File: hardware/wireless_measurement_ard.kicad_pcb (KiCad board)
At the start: 4 copper layers, 30.3 x 17.8 mm, 25 parts, among them J1 Conn_01x08, SW1 SW_SPDT, U1 EFM8LB1, U2 JDY-08, U3 MCP16415, U4 MAX44284, U5 DRV5021

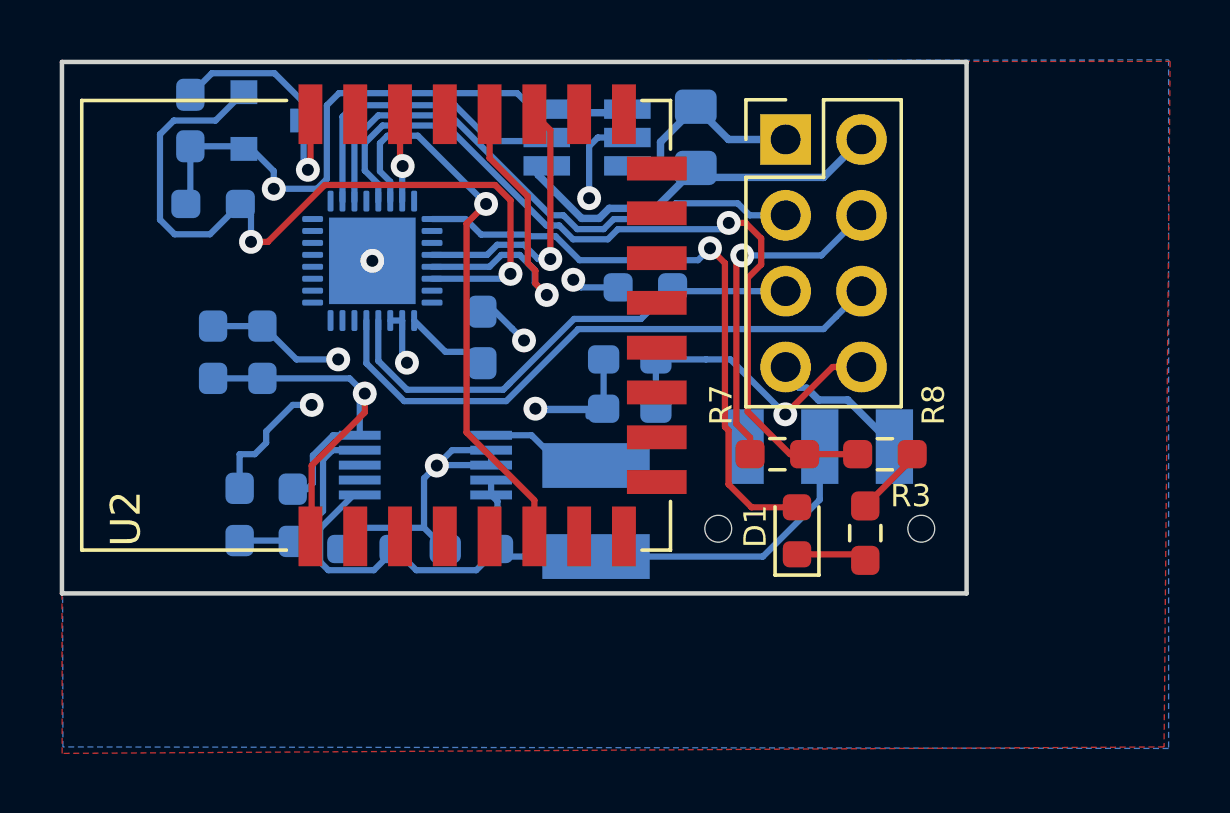
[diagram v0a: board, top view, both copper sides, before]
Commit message: Rerouting to remove components below antenna
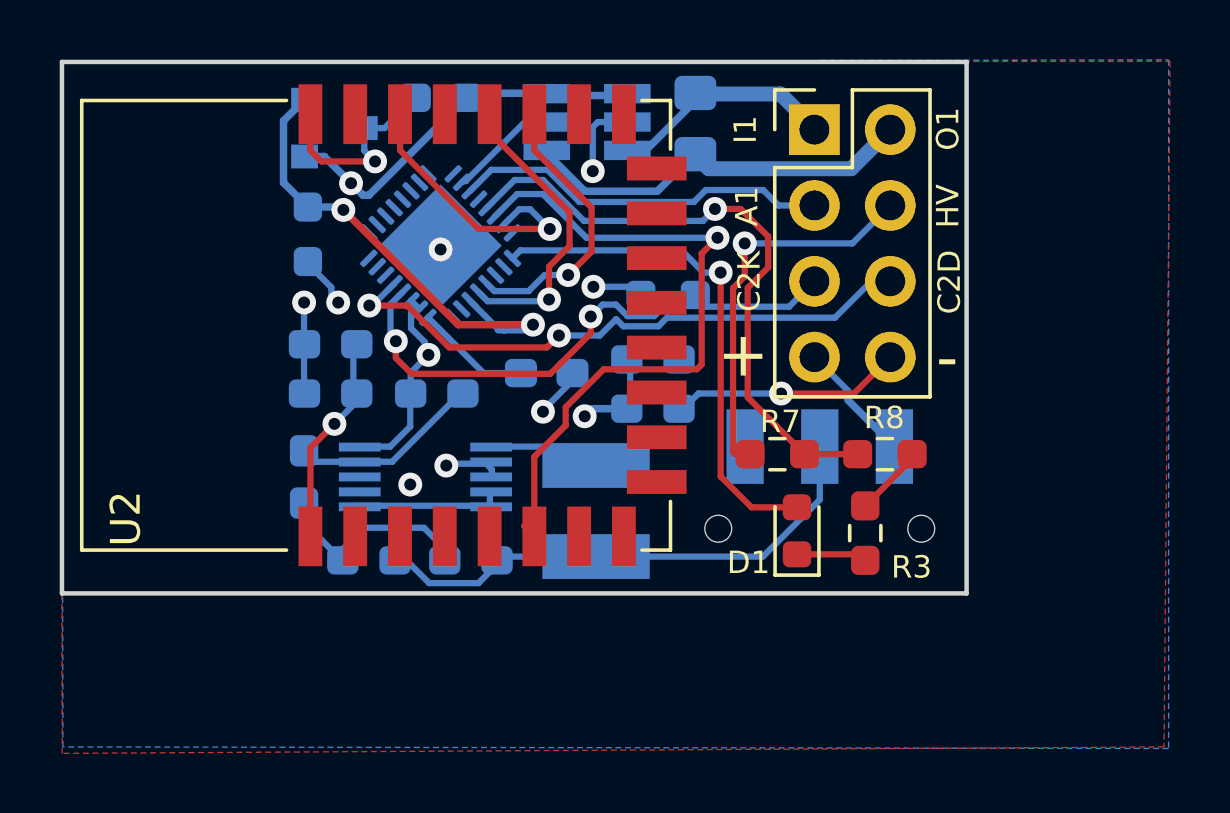
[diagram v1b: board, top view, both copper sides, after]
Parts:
- moved C8 8.42 mm to (122.7, 76.2), turned to 180 degrees
- moved R4 6.32 mm to (122.6, 86.1), turned to 180 degrees
- moved C5 3.95 mm to (119.0, 84.5), turned to 180 degrees
- moved R2 3.33 mm to (118.2, 80.8), turned to 90 degrees
- moved C6 2.67 mm to (119.0, 86.1), turned to 180 degrees
- moved R5 2.50 mm to (118.1, 88.9), turned to 90 degrees
- moved C7 2.47 mm to (126.2, 85.4), turned to 180 degrees
- moved U1 2.34 mm to (122.7, 81.2), turned to 45 degrees
- moved U5 2.05 mm to (119.1, 77.2)
- moved J1 1.02 mm to (135.2, 77.3)
- moved R6 0.80 mm to (130.3, 82.8)
- moved C1 0.78 mm to (129.8, 86.6)
- moved C2 0.78 mm to (129.8, 85.0)
- moved U4 0.52 mm to (127.6, 77.0)
- moved R1 0.46 mm to (131.2, 77.1)
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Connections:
- U2 pad 3: Net-(U2-Pad3) -> GND
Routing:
- net GND: track 46.3 -> 32.7 mm
- net +3V3: track 46.3 -> 34.5 mm, vias 5 -> 6
- net HALL_PIN: track 25.8 -> 16.2 mm
- net A3: track 27.9 -> 21.1 mm
- net PWRC: track 2.95 -> 9.34 mm
- net A0: track 10.0 -> 3.67 mm
- net A1: track 18.9 -> 12.7 mm
- net STATUS: track 19.0 -> 23.3 mm
- net LED: track 20.8 -> 17.2 mm
- net C2CK: track 17.0 -> 18.9 mm, vias 0 -> 2
- net ARD_TX: track 11.9 -> 10.1 mm
- net VHIGH: track 11.5 -> 13.1 mm
- net BATT: track 5.39 -> 4.11 mm
- net Net-(C7-Pad2): track 2.72 -> 3.89 mm
- net Net-(L1-Pad2): track 6.96 -> 7.85 mm
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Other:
- board text added: "HV"
- board text removed: "VH"

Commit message: label changes
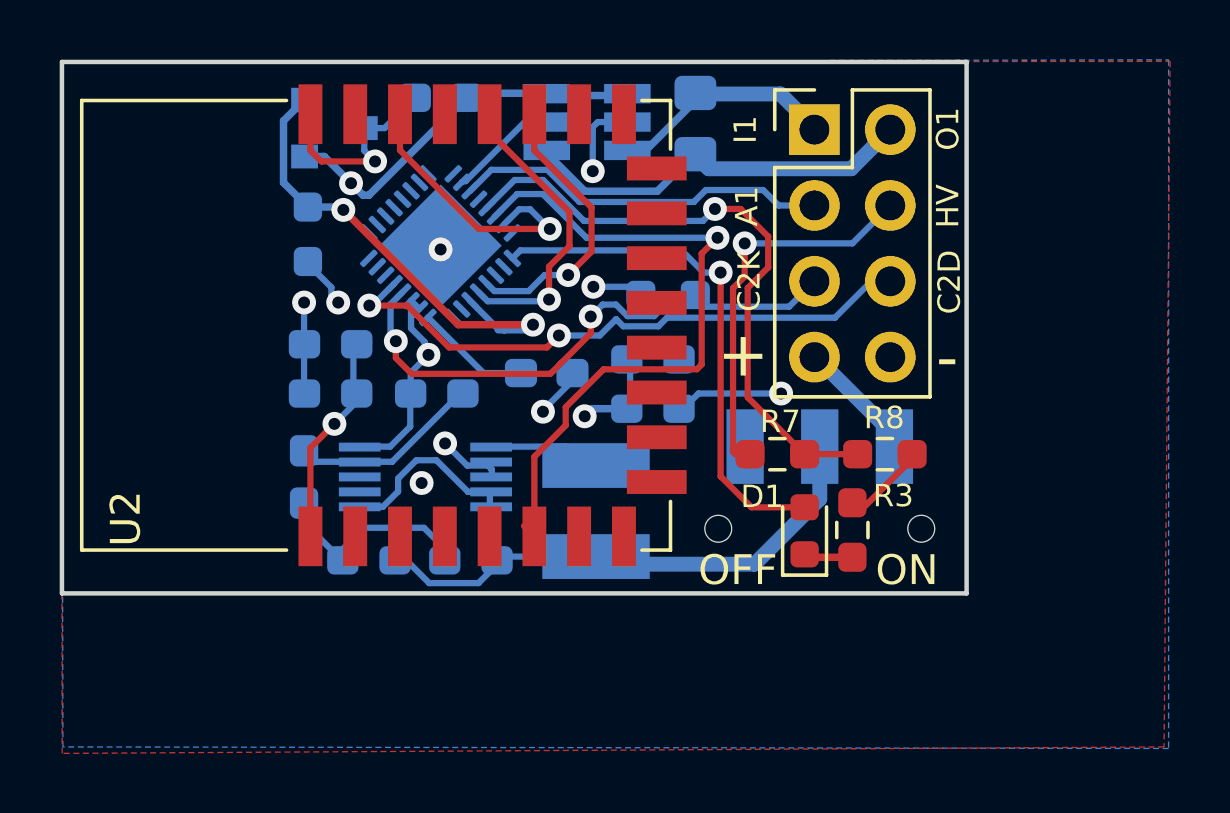
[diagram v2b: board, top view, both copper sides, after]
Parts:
- moved R3 0.44 mm to (136.5, 90.7)
- moved D1 0.25 mm to (134.9, 90.7)
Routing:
- net GND: track 32.7 -> 28.9 mm
- net VIN: track 24.9 -> 26.5 mm
- net Net-(D1-Pad1): track 2.37 -> 1.64 mm
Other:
- board text added: "OFF"
- board text added: "ON"
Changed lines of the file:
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@@
   (general
     (thickness 1.6)
-    (drawings 13)
-    (tracks 262)
+    (drawings 15)
+    (tracks 267)
     (zones 0)
     (modules 25)
@@
   )
   (setup
-    (last_trace_width 0.21)
+    (last_trace_width 0.25)
     (user_trace_width 0.21)
     (user_trace_width 0.5)
@@
     (pad_to_mask_clearance 0)
     (aux_axis_origin 0 0)
-    (visible_elements 7FFFFDFF)
+    (visible_elements 7FFFFFFF)
     (pcbplotparams
       (layerselection 0x010fc_ffffffff)
@@
   )
   (module Resistor_SMD:R_0603_1608Metric_Pad0.98x0.95mm_HandSolder (layer F.Cu)
-    (at 136.906 90.7815 90)
+    (at 136.4742 90.678 90)
     (descr "Resistor SMD 0603 (1608 Metric), square (rectangular) end terminal, IPC_7351 nominal with elongated pad for handsoldering. (Body size source: IPC-SM-782 page 72, https://www.pcb-3d.com/wordpress/wp-content/uploads/ipc-sm-782a_amendment_1_and_2.pdf), generated with kicad-footprint-generator")
     (tags "resistor handsolder")
     (attr smd)
-    (fp_text reference R3 (at -1.1411 1.5494 180) (layer F.SilkS)
+    (fp_text reference R3 (at 1.1449 1.3716 180) (layer F.SilkS)
       (effects (font (size 0.75 0.75) (thickness 0.15)))
     )
@@
   )
   (module LED_SMD:LED_0603_1608Metric (layer F.Cu)
-    (at 134.62 90.7035 90)
+    (at 134.874 90.7035 90)
     (descr "LED SMD 0603 (1608 Metric), square (rectangular) end terminal, IPC_7351 nominal, (Body size source: http://www.tortai-tech.com/upload/download/2011102023233369053.pdf), generated with kicad-footprint-generator")
     (tags diode)
     (attr smd)
-    (fp_text reference D1 (at -1.0667 -1.6256) (layer F.SilkS)
+    (fp_text reference D1 (at 1.1431 -1.4224) (layer F.SilkS)
       (effects (font (size 0.75 0.75) (thickness 0.15)))
     )
@@
     )
   )
+  (gr_text OFF (at 132.6388 92.0242) (layer F.SilkS)
+    (effects (font (size 1 1) (thickness 0.25)))
+  )
+  (gr_text ON (at 138.303 92.0242) (layer F.SilkS)
+    (effects (font (size 1 1) (thickness 0.25)))
+  )
   (gr_text - (at 139.6492 84.9122) (layer F.SilkS)
     (effects (font (size 1.5 1.5) (thickness 0.3)))
@@
   (gr_line (start 140.3 75) (end 140.3 92.8) (layer Edge.Cuts) (width 0.15))
   (gr_line (start 110 75) (end 140.3 75) (layer Edge.Cuts) (width 0.15))
-  (via (at 121.666 89.154) (size 0.8) (drill 0.4) (layers F.Cu B.Cu) (net 1))
+  (via (at 122.047 89.1032) (size 0.8) (drill 0.4) (layers F.Cu B.Cu) (net 1))
   (via (at 122.682 81.28) (size 0.8) (drill 0.4) (layers F.Cu B.Cu) (net 1))
   (segment (start 138.477 88.298) (end 136.906 89.869) (width 0.21) (layer F.Cu) (net 1))
@@
   (segment (start 120.11801 90.60299) (end 122.12699 90.60299) (width 0.21) (layer B.Cu) (net 1))
   (segment (start 119.408 91.313) (end 120.11801 90.60299) (width 0.21) (layer B.Cu) (net 1))
-  (segment (start 124.333 88.4555) (end 123.1265 88.4555) (width 0.21) (layer B.Cu) (net 1))
-  (via (at 122.8725 88.519) (size 0.8) (drill 0.4) (layers F.Cu B.Cu) (net 1))
-  (segment (start 123.063 88.519) (end 122.8725 88.519) (width 0.21) (layer B.Cu) (net 1))
-  (segment (start 123.1265 88.4555) (end 123.063 88.519) (width 0.21) (layer B.Cu) (net 1))
   (segment (start 124.3965 88.646) (end 124.2695 88.519) (width 0.21) (layer B.Cu) (net 1))
   (segment (start 124.3965 88.9) (end 124.3965 88.646) (width 0.21) (layer B.Cu) (net 1))
@@
   (segment (start 131.318004 86.105996) (end 134.0866 86.105996) (width 0.21) (layer B.Cu) (net 1))
   (segment (start 130.81 86.614) (end 131.318004 86.105996) (width 0.21) (layer B.Cu) (net 1))
-  (segment (start 137.7442 84.8868) (end 136.525004 86.105996) (width 0.21) (layer F.Cu) (net 1))
-  (segment (start 136.525004 86.105996) (end 134.0866 86.105996) (width 0.21) (layer F.Cu) (net 1))
+  (segment (start 124.333 88.4555) (end 124.2695 88.519) (width 0.21) (layer B.Cu) (net 1))
+  (via (at 122.832115 87.776234) (size 0.8) (drill 0.4) (layers F.Cu B.Cu) (net 1))
+  (segment (start 124.2695 88.519) (end 123.574881 88.519) (width 0.21) (layer B.Cu) (net 1))
+  (segment (start 123.574881 88.519) (end 122.832115 87.776234) (width 0.21) (layer B.Cu) (net 1))
   (segment (start 125.161389 78.953011) (end 126.114327 78.953011) (width 0.21) (layer B.Cu) (net 2))
   (segment (start 127.485802 80.324486) (end 131.470343 80.324486) (width 0.21) (layer B.Cu) (net 2))
@@
   (segment (start 123.954792 82.708635) (end 124.261613 83.015456) (width 0.21) (layer B.Cu) (net 8))
   (segment (start 126.3142 81.853492) (end 126.3142 82.9564) (width 0.21) (layer F.Cu) (net 8))
-  (segment (start 135.382 87.884) (end 135.382 89.662) (width 0.21) (layer B.Cu) (net 9))
-  (segment (start 133.477 91.567) (end 127.889 91.567) (width 0.21) (layer B.Cu) (net 9))
-  (segment (start 135.382 89.662) (end 133.477 91.567) (width 0.21) (layer B.Cu) (net 9))
   (segment (start 124.841 91.567) (end 124.587 91.313) (width 0.21) (layer B.Cu) (net 9))
   (segment (start 127.889 91.567) (end 124.841 91.567) (width 0.21) (layer B.Cu) (net 9))
@@
   (segment (start 124.333 89.8525) (end 124.333 89.4715) (width 0.21) (layer B.Cu) (net 9))
   (segment (start 124.333 89.8652) (end 124.3838 89.916) (width 0.21) (layer B.Cu) (net 9))
-  (segment (start 119.9388 89.8652) (end 124.333 89.8652) (width 0.21) (layer B.Cu) (net 9))
+  (segment (start 128.143 91.821) (end 127.889 91.567) (width 0.5) (layer B.Cu) (net 9))
+  (segment (start 133.195 91.821) (end 128.143 91.821) (width 0.5) (layer B.Cu) (net 9))
+  (segment (start 135.382 89.634) (end 133.195 91.821) (width 0.5) (layer B.Cu) (net 9))
+  (segment (start 135.382 87.884) (end 135.382 89.634) (width 0.5) (layer B.Cu) (net 9))
+  (segment (start 122.542198 88.3412) (end 123.600998 89.4) (width 0.21) (layer B.Cu) (net 9))
+  (segment (start 121.869198 88.3412) (end 122.542198 88.3412) (width 0.21) (layer B.Cu) (net 9))
+  (segment (start 121.2596 89.387402) (end 121.2596 88.950798) (width 0.21) (layer B.Cu) (net 9))
+  (segment (start 120.747002 89.9) (end 121.2596 89.387402) (width 0.21) (layer B.Cu) (net 9))
+  (segment (start 119.974 89.9) (end 120.747002 89.9) (width 0.21) (layer B.Cu) (net 9))
+  (segment (start 123.600998 89.4) (end 124.374 89.4) (width 0.21) (layer B.Cu) (net 9))
+  (segment (start 121.2596 88.950798) (end 121.869198 88.3412) (width 0.21) (layer B.Cu) (net 9))
   (segment (start 126.238 78.056572) (end 126.238 77.9526) (width 0.25) (layer B.Cu) (net 10))
   (segment (start 129.940605 79.329995) (end 127.511422 79.329995) (width 0.25) (layer B.Cu) (net 10))
@@
   (segment (start 134.354201 83.196799) (end 131.558399 83.196799) (width 0.21) (layer B.Cu) (net 16))
   (segment (start 135.2042 82.3468) (end 134.354201 83.196799) (width 0.21) (layer B.Cu) (net 16))
-  (segment (start 136.703 91.491) (end 136.906 91.694) (width 0.21) (layer F.Cu) (net 17))
-  (segment (start 134.62 91.491) (end 136.703 91.491) (width 0.21) (layer F.Cu) (net 17))
-  (segment (start 136.320001 86.322001) (end 137.882 87.884) (width 0.25) (layer B.Cu) (net 18))
-  (segment (start 136.320001 86.002601) (end 136.320001 86.322001) (width 0.21) (layer B.Cu) (net 18))
-  (segment (start 135.2042 84.8868) (end 136.320001 86.002601) (width 0.21) (layer B.Cu) (net 18))
+  (segment (start 134.9735 91.5905) (end 134.874 91.491) (width 0.25) (layer F.Cu) (net 17))
+  (segment (start 136.4742 91.5905) (end 134.9735 91.5905) (width 0.25) (layer F.Cu) (net 17))
+  (segment (start 137.882 87.5138) (end 137.882 87.884) (width 0.5) (layer B.Cu) (net 18))
+  (segment (start 135.255 84.8868) (end 137.882 87.5138) (width 0.5) (layer B.Cu) (net 18))
+  (segment (start 135.2042 84.8868) (end 135.255 84.8868) (width 0.5) (layer B.Cu) (net 18))
   (segment (start 134.62 89.916) (end 133.096 89.916) (width 0.21) (layer F.Cu) (net 19))
   (via (at 132.061823 82.054502) (size 0.8) (drill 0.4) (layers F.Cu B.Cu) (net 19))

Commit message: Added some markings
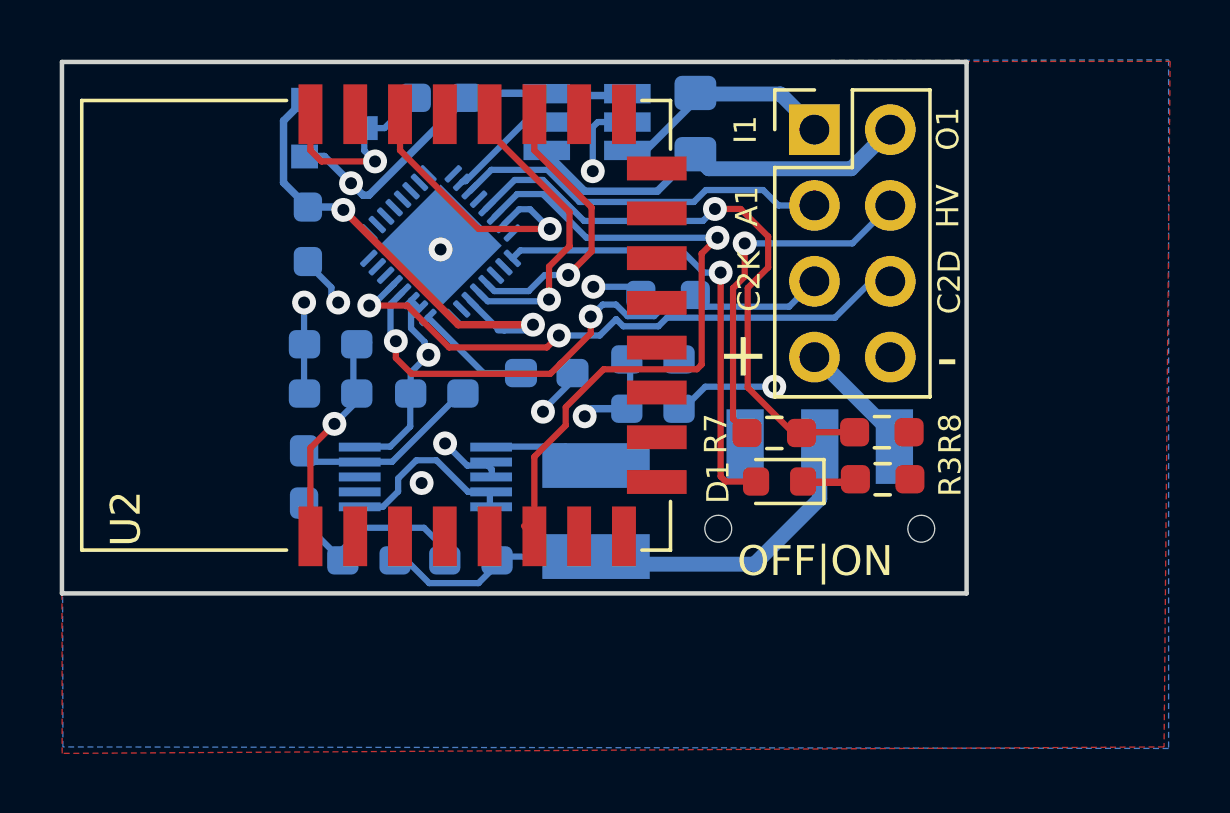
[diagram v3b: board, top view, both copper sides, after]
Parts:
- moved R3 1.98 mm to (137.5, 89.0), turned to 0 degrees
- moved D1 1.85 mm to (134.0, 89.1), turned to 180 degrees
- moved R8 0.74 mm to (137.5, 87.4)
- moved R7 0.72 mm to (133.9, 87.4)
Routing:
- net GND: track 28.9 -> 26.4 mm
- net LED: track 17.2 -> 15.5 mm
- net VHIGH: track 13.1 -> 12.1 mm
- net A3: track 21.1 -> 20.5 mm
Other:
- board text added: "OFF|ON"
- board text removed: "OFF"
- board text removed: "ON"

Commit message: Added icon
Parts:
- added Ref**: Val**, img:drawing, F.Cu at (113.9, 77.8)
